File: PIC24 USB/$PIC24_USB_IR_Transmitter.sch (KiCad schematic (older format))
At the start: 35 parts, among them CON1 USB-MINI-B, P1 CONN_6, P2 CONN_4, P3 CONN_4, P4 CONN_8, P5 CONN_4, P6 CONN_1, P7 CONN_8, P8 CONN_8X2, Q1 2N7002, U2 LM1117_SOT223_3V3, U4 MCP48X2, U5 MCP9700, U6 24C16

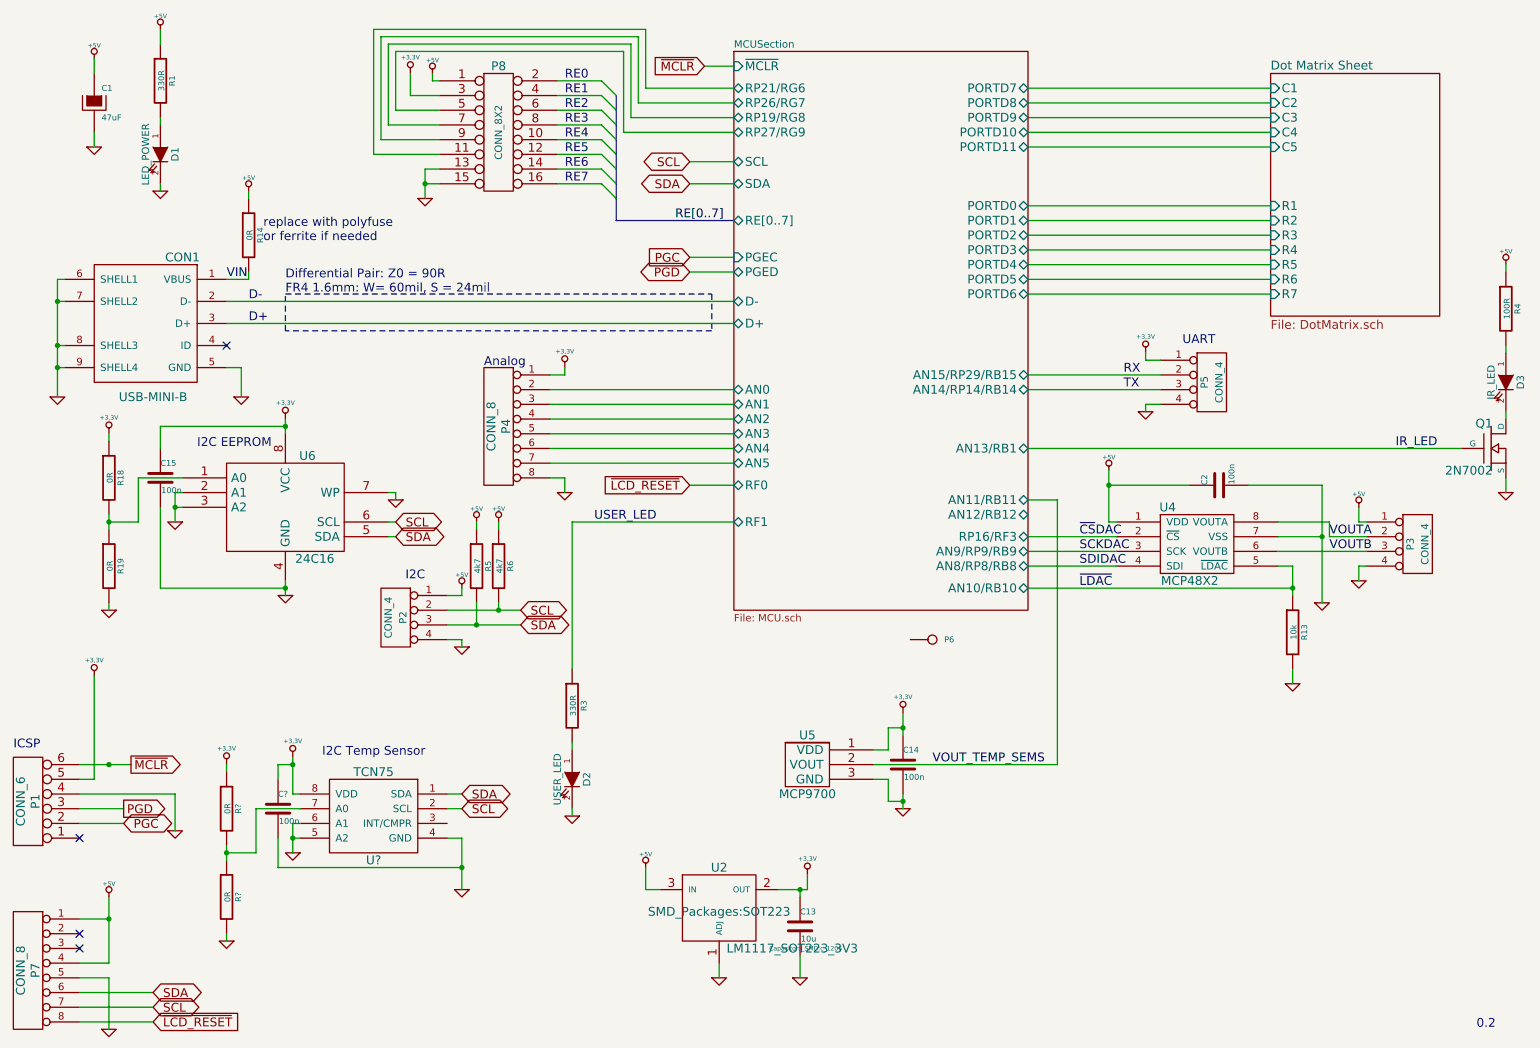
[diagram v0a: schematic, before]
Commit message: added I2C Temp sensor and eeprom
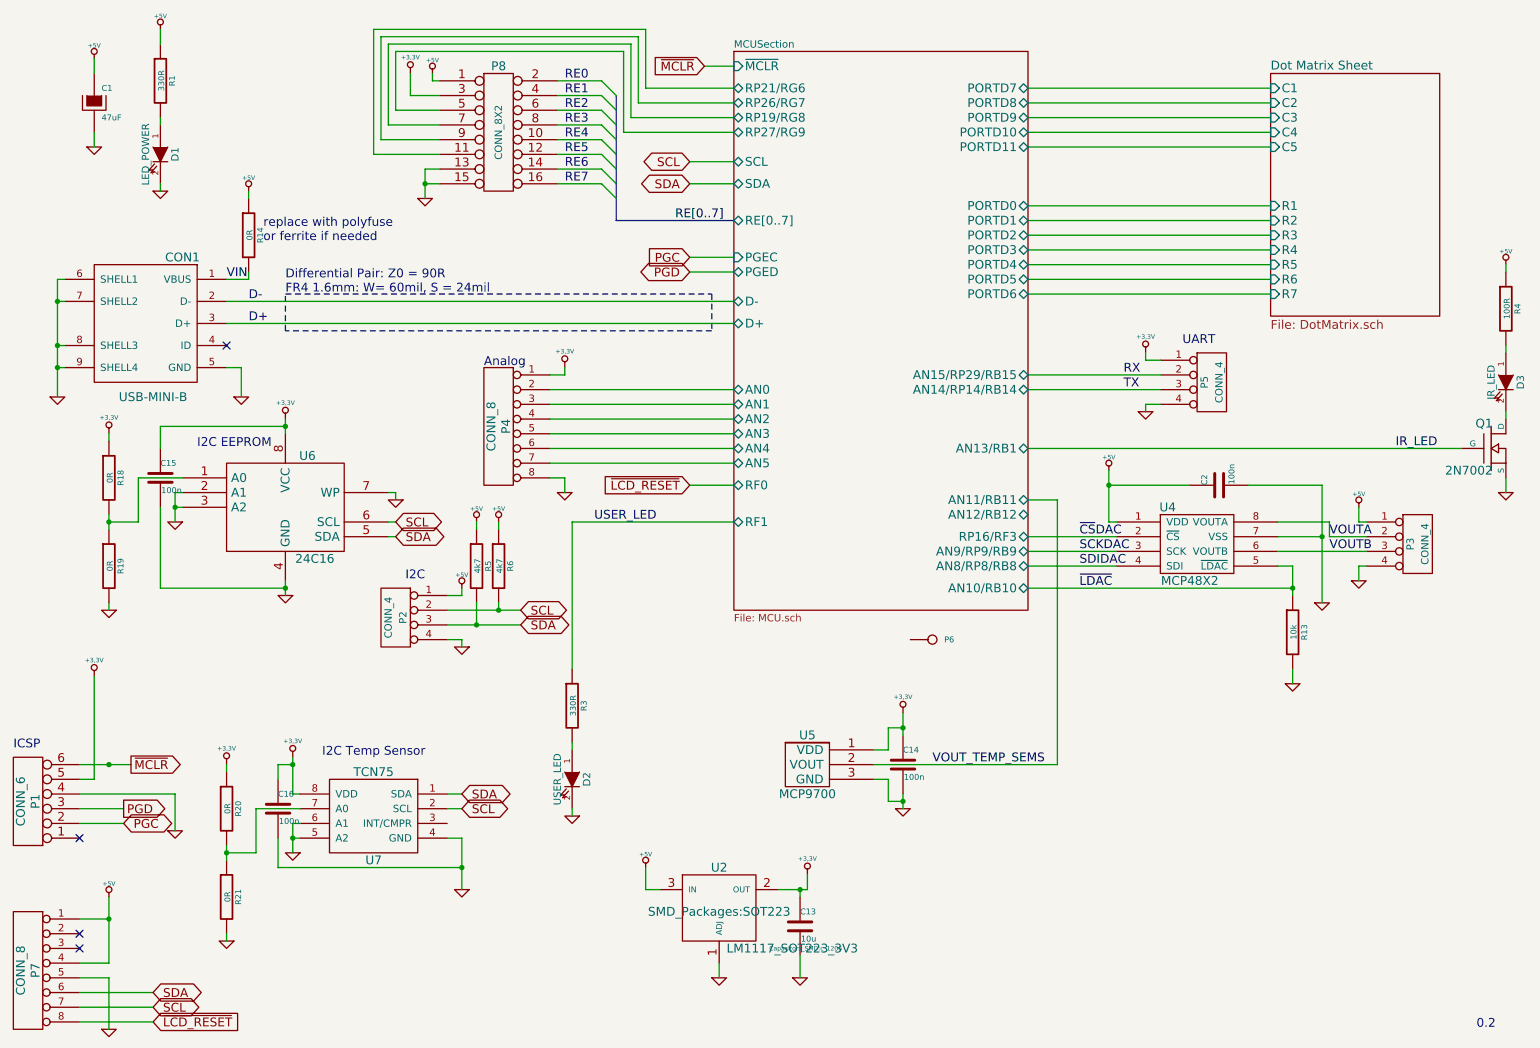
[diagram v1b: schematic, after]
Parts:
- U7: renamed from U?; footprint (none) -> SMD_Packages:SOIC-8-N
- gave numbers to parts that had none: 3
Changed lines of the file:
@@
 $EndDescr
 Wire Wire Line
-	950  2550 950  2700
-Wire Wire Line
-	950  2700 950  3000
-Wire Wire Line
-	950  3000 950  3150
-Wire Wire Line
-	950  3150 950  3350
+	950  2550 950  3350
 Wire Wire Line
 	950  2550 1000 2550
@@
 ~MCLR~
 Wire Wire Line
-	1100 5850 1300 5850
-Wire Wire Line
-	1300 5850 1450 5850
+	1100 5850 1450 5850
 Wire Wire Line
 	1100 5950 1200 5950
@@
 $EndComp
 Wire Wire Line
-	1300 6750 1300 6900
-Wire Wire Line
-	1300 6900 1300 7200
+	1300 6750 1300 7200
 Wire Wire Line
 	1300 6900 1100 6900
@@
 	5550 3950 5250 3950
 Wire Wire Line
-	3600 4800 3950 4800
-Wire Wire Line
-	3950 4800 4100 4800
-Wire Wire Line
-	3600 4900 3800 4900
-Wire Wire Line
-	3800 4900 4100 4900
+	3600 4800 4100 4800
+Wire Wire Line
+	3600 4900 4100 4900
 Wire Wire Line
 	7550 3200 8450 3200
@@
 	4950 6700 4950 6550
 Wire Wire Line
-	5850 6700 6000 6700
-Wire Wire Line
-	6000 6700 6050 6700
+	5850 6700 6050 6700
 Wire Wire Line
 	6050 6700 6050 6600
@@
 	4650 1900 4750 2000
 Wire Bus Line
-	4750 1300 4750 1400
-Wire Bus Line
-	4750 1400 4750 1500
-Wire Bus Line
-	4750 1500 4750 1600
-Wire Bus Line
-	4750 1600 4750 1700
-Wire Bus Line
-	4750 1700 4750 1800
-Wire Bus Line
-	4750 1800 4750 1900
-Wire Bus Line
-	4750 1900 4750 2000
-Wire Bus Line
-	4750 2000 4750 2150
+	4750 1300 4750 2150
 Text Label 4400 1300 0    60   ~ 0
 RE1
@@
 	3550 1900 3450 1900
 Wire Wire Line
-	3450 1800 3450 1900
-Wire Wire Line
-	3450 1900 3450 2000
+	3450 1800 3450 2000
 Wire Wire Line
 	3550 1800 3450 1800
@@
 	8100 4200 8150 4200
 Wire Wire Line
-	8100 3850 8100 3950
-Wire Wire Line
-	8100 3950 8100 4200
-Wire Wire Line
-	9550 3950 9550 4300
-Wire Wire Line
-	9550 4300 9550 4750
+	8100 3850 8100 4200
+Wire Wire Line
+	9550 3950 9550 4750
 $Comp
 L GND #PWR028
@@
 	9250 4500 9350 4500
 Wire Wire Line
-	9350 4500 9350 4650
-Wire Wire Line
-	9350 4650 9350 4700
+	9350 4500 9350 4700
 Wire Wire Line
 	7550 4650 9350 4650
@@
 	6600 5600 6700 5600
 Wire Wire Line
-	6700 5500 6700 5600
-Wire Wire Line
-	6700 5600 6700 5650
+	6700 5500 6700 5650
 Connection ~ 6700 5600
 Wire Wire Line
@@
 	6600 6100 6700 6100
 Wire Wire Line
-	6700 6050 6700 6100
-Wire Wire Line
-	6700 6100 6700 6150
+	6700 6050 6700 6150
 Connection ~ 6700 6100
 Text Notes 10600 7650 0    60   ~ 0
@@
 $EndComp
 Wire Wire Line
-	2500 4600 2500 4650
-Wire Wire Line
-	2500 4650 2500 4700
+	2500 4600 2500 4700
 $Comp
 L +3,3V #PWR038
@@
 $EndComp
 Wire Wire Line
-	2500 3500 2500 3550
-Wire Wire Line
-	2500 3550 2500 3600
+	2500 3500 2500 3600
 Text GLabel 3250 4300 2    60   BiDi ~ 0
 SDA
@@
 $EndComp
 Wire Wire Line
-	1750 4000 1750 4100
-Wire Wire Line
-	1750 4100 1750 4200
+	1750 4000 1750 4200
 Wire Wire Line
 	1750 4100 1800 4100
@@
 	1300 4800 1300 4750
 Wire Wire Line
-	1300 4150 1300 4200
-Wire Wire Line
-	1300 4200 1300 4250
+	1300 4150 1300 4250
 Wire Wire Line
 	1300 4200 1500 4200
@@
 I2C EEPROM
 $Comp
-L TCN75 U?
+L TCN75 U7
 U 1 1 5464A69F
 P 3100 6150
-F 0 "U?" H 3100 5800 60  0000 C CNN
+F 0 "U7" H 3100 5800 60  0000 C CNN
 F 1 "TCN75" H 3100 6400 60  0000 C CNN
-F 2 "" H 3100 5800 60  0000 C CNN
+F 2 "SMD_Packages:SOIC-8-N" H 3100 5800 60  0001 C CNN
 F 3 "" H 3100 5800 60  0000 C CNN
 	1    3100 6150
@@
 	3600 6150 3700 6150
 $Comp
-L GND #PWR?
+L GND #PWR043
 U 1 1 5464ADEE
 P 3700 6700
-F 0 "#PWR?" H 3700 6700 30  0001 C CNN
+F 0 "#PWR043" H 3700 6700 30  0001 C CNN
 F 1 "GND" H 3700 6630 30  0001 C CNN
 F 2 "" H 3700 6700 60  0000 C CNN
@@
 $EndComp
 $Comp
-L GND #PWR?
+L GND #PWR044
 U 1 1 5464AED8
 P 2550 6450
-F 0 "#PWR?" H 2550 6450 30  0001 C CNN
+F 0 "#PWR044" H 2550 6450 30  0001 C CNN
 F 1 "GND" H 2550 6380 30  0001 C CNN
 F 2 "" H 2550 6450 60  0000 C CNN
@@
 $EndComp
 $Comp
-L +3,3V #PWR?
+L +3,3V #PWR045
 U 1 1 5464AF03
 P 2550 5800
-F 0 "#PWR?" H 2550 5760 30  0001 C CNN
+F 0 "#PWR045" H 2550 5760 30  0001 C CNN
 F 1 "+3,3V" H 2550 5910 30  0000 C CNN
 F 2 "" H 2550 5800 60  0000 C CNN
@@
 	3600 6350 3700 6350
 Wire Wire Line
-	3700 6350 3700 6550
-Wire Wire Line
-	3700 6550 3700 6700
+	3700 6350 3700 6700
 Wire Wire Line
 	2550 6050 2600 6050
 Wire Wire Line
-	2550 5800 2550 5850
-Wire Wire Line
-	2550 5850 2550 6050
+	2550 5800 2550 6050
 Wire Wire Line
 	2600 6250 2550 6250
 Wire Wire Line
-	2550 6250 2550 6350
-Wire Wire Line
-	2550 6350 2550 6450
+	2550 6250 2550 6450
 Wire Wire Line
 	2600 6350 2550 6350
@@
 Connection ~ 3700 6550
 $Comp
-L R R?
+L R R20
 U 1 1 54651E19
 P 2100 6150
-F 0 "R?" V 2180 6150 40  0000 C CNN
+F 0 "R20" V 2180 6150 40  0000 C CNN
 F 1 "0R" V 2107 6151 40  0000 C CNN
 F 2 "SMD_Packages:SMD-0603_r" V 2030 6150 30  0001 C CNN
@@
 $EndComp
 $Comp
-L R R?
+L R R21
 U 1 1 54651E1F
 P 2100 6750
-F 0 "R?" V 2180 6750 40  0000 C CNN
+F 0 "R21" V 2180 6750 40  0000 C CNN
 F 1 "0R" V 2107 6751 40  0000 C CNN
 F 2 "SMD_Packages:SMD-0603_r" V 2030 6750 30  0001 C CNN
@@
 $EndComp
 $Comp
-L GND #PWR?
+L GND #PWR046
 U 1 1 54651E25
 P 2100 7050
-F 0 "#PWR?" H 2100 7050 30  0001 C CNN
+F 0 "#PWR046" H 2100 7050 30  0001 C CNN
 F 1 "GND" H 2100 6980 30  0001 C CNN
 F 2 "" H 2100 7050 60  0000 C CNN
@@
 	2100 7050 2100 7000
 Wire Wire Line
-	2100 6400 2100 6450
-Wire Wire Line
-	2100 6450 2100 6500
+	2100 6400 2100 6500
 Wire Wire Line
 	2100 6450 2300 6450
@@
 Connection ~ 2100 6450
 $Comp
-L +3,3V #PWR?
+L +3,3V #PWR047
 U 1 1 54651E32
 P 2100 5850
-F 0 "#PWR?" H 2100 5810 30  0001 C CNN
+F 0 "#PWR047" H 2100 5810 30  0001 C CNN
 F 1 "+3,3V" H 2100 5960 30  0000 C CNN
 F 2 "" H 2100 5850 60  0000 C CNN
@@
 	2100 5900 2100 5850
 $Comp
-L C C?
+L C C16
 U 1 1 54651E39
 P 2450 6150
-F 0 "C?" H 2450 6250 40  0000 L CNN
+F 0 "C16" H 2450 6250 40  0000 L CNN
 F 1 "100n" H 2456 6065 40  0000 L CNN
 F 2 "SMD_Packages:SMD-0603_c" H 2488 6000 30  0001 C CNN
